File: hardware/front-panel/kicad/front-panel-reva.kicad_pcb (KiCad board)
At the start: 2 copper layers, 184 x 62.3 mm, 35 parts, among them J1 UI_LINK / IDC 2x8 2.54mm, U1 TCA9534PWR

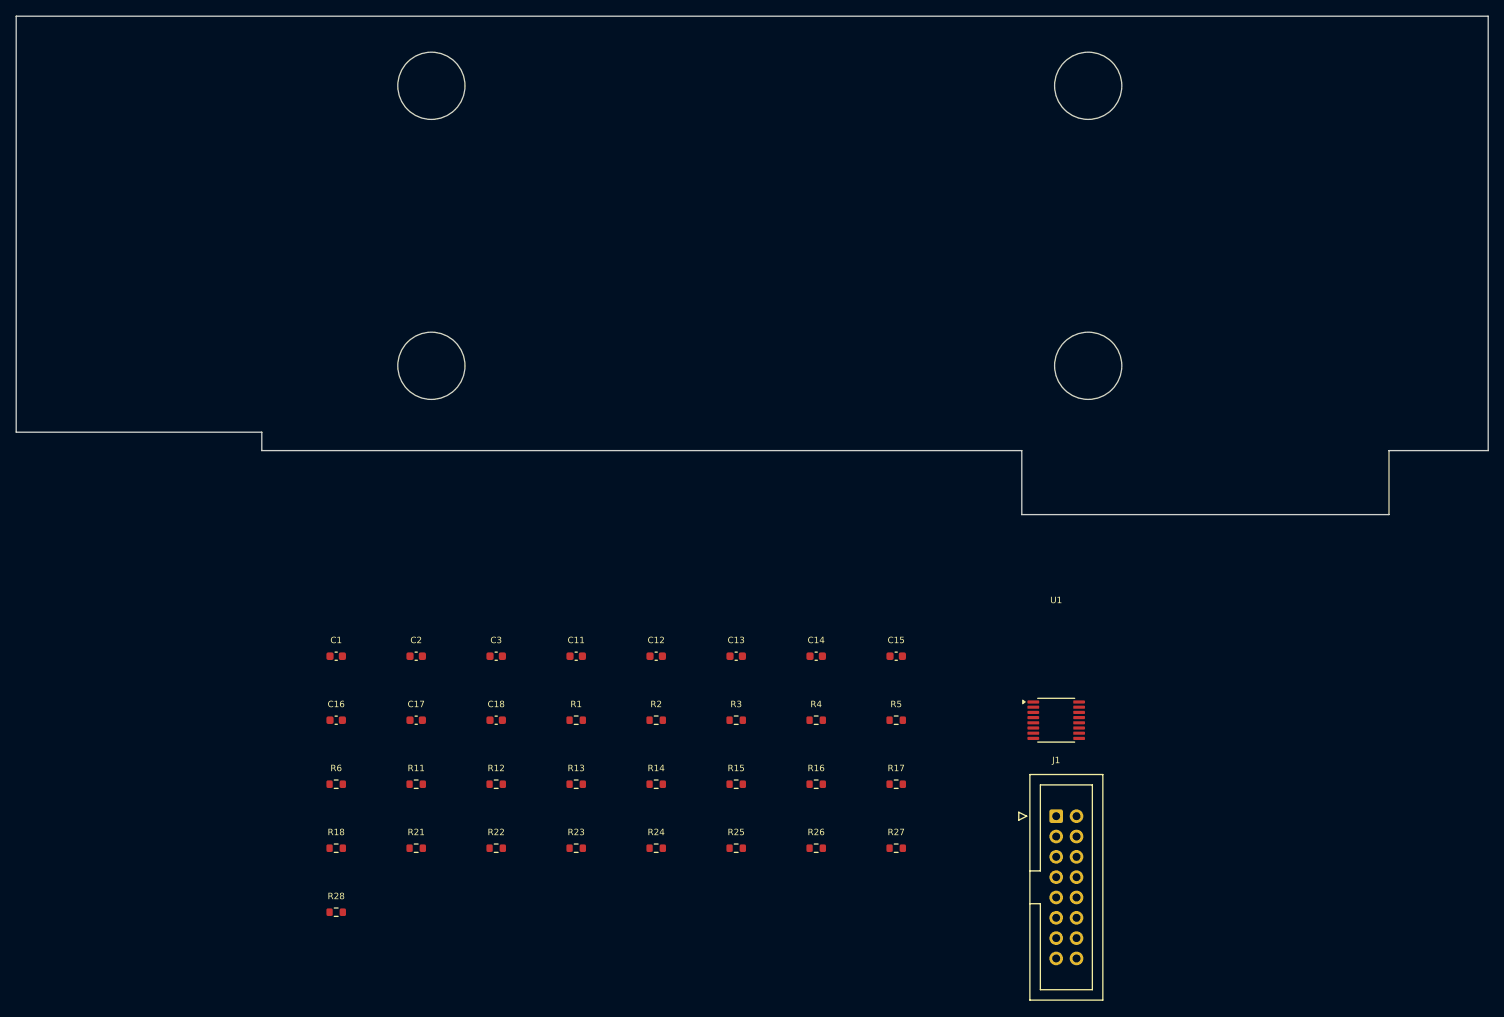
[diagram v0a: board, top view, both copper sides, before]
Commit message: Lay out and route the front panel PCB for JLCPCB
Assign JLC parts to the open positions: HRO K2-1102SP-A4SC-04 6x6x4.3 mm
switches (C83916) with a project footprint from the EasyEDA land pattern,
JST S8B-PH-K-S for J2 in the Waveshare cable order (C157915), and the
standby LED on TCA9534 P7 (KT-0603R + 470R). Seven key channels replace
the eighth, whose parts are removed from schematic and board.

layout_front_panel_pcb.py places the parts on the measured positions,
routes with Freerouting 2.4.1 through Specctra DSN/SES and pours GND on
both layers with stitching and island anchoring. KiCad 10.0.6 DRC with
schematic parity and all severities: 0 violations, 0 unconnected, 0
parity issues. export_front_panel_fab.py writes Gerbers, drill, BOM and
CPL for JLCPCB; the package stays a candidate pending the checks listed
in hardware/front-panel/layout.md.

Co-Authored-By: Claude Opus 5 <noreply@anthropic.com>
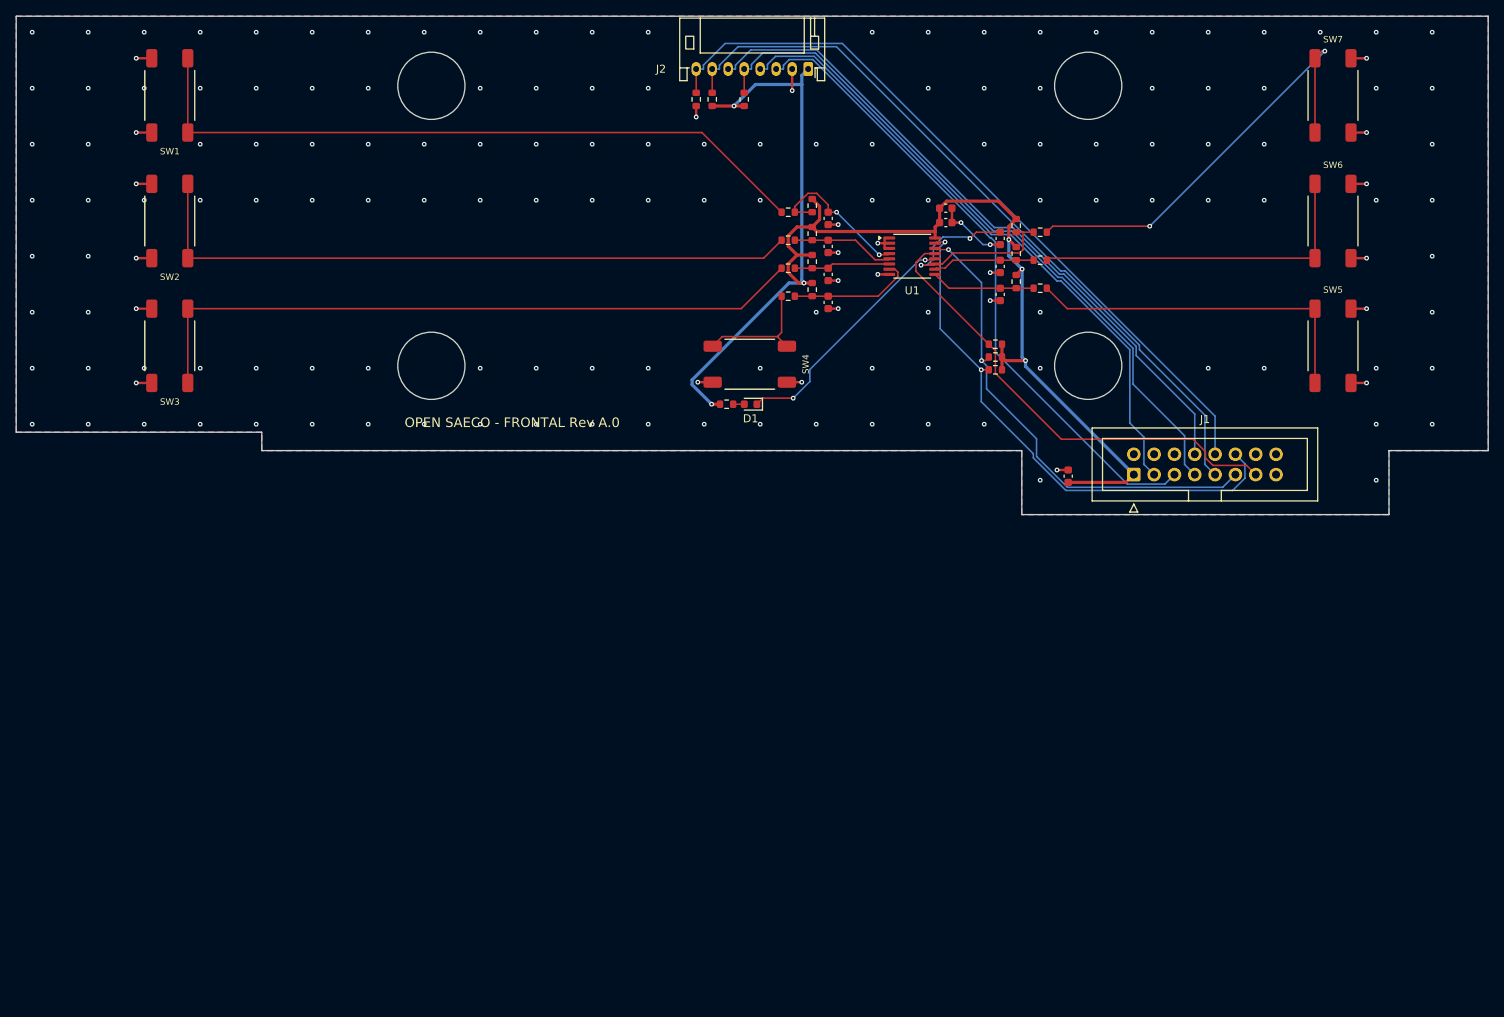
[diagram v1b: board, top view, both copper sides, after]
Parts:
- removed C18: 100nF / filtro, Capacitor_SMD:C_0603_1608Metric
- removed R18: 10k / pull-up, Resistor_SMD:R_0603_1608Metric
- removed R28: 1k / serie, Resistor_SMD:R_0603_1608Metric
- added D1: KT-0603R / STBY, LED_SMD:LED_0603_1608Metric, F.Cu at (91.8, 48.5)
- added J2: LCD_ADAPTER / JST PH 8, Connector_JST:JST_PH_S8B-PH-K_1x08_P2.00mm_Horizontal, F.Cu at (99.0, 6.60)
- added R7: 470 / LED, Resistor_SMD:R_0603_1608Metric, F.Cu at (88.8, 48.5)
- added SW1: KEY 1 / PB1, OpenSaeco:SW_HRO_K2-1102SP-A4SC-04, F.Cu at (19.2, 9.90)
- added SW2: KEY 2 / PB2, OpenSaeco:SW_HRO_K2-1102SP-A4SC-04, F.Cu at (19.2, 25.6)
- added SW3: KEY 3 / PB3, OpenSaeco:SW_HRO_K2-1102SP-A4SC-04, F.Cu at (19.2, 41.2)
- added SW4: KEY 4 / PB8, OpenSaeco:SW_HRO_K2-1102SP-A4SC-04, F.Cu at (91.7, 43.5)
- added SW5: KEY 5 / PB4/PB6, OpenSaeco:SW_HRO_K2-1102SP-A4SC-04, F.Cu at (164.6, 41.2)
- added SW6: KEY 6 / PB5, OpenSaeco:SW_HRO_K2-1102SP-A4SC-04, F.Cu at (164.6, 25.6)
- added SW7: KEY 7 / PB7, OpenSaeco:SW_HRO_K2-1102SP-A4SC-04, F.Cu at (164.6, 9.90)
- moved C16 100.5 mm to (123.0, 31.3), turned to -90 degrees
- moved R6 96.7 mm to (85.0, 10.4), turned to -90 degrees
- moved C17 94.6 mm to (123.0, 27.8), turned to -90 degrees
- moved C1 93.5 mm to (116.2, 25.8)
- moved R21 92.1 mm to (96.5, 24.5), turned to 180 degrees
- moved R11 87.6 mm to (99.5, 23.7), turned to -90 degrees
- moved C2 86.7 mm to (116.2, 24.0)
- moved R22 84.3 mm to (96.5, 28.0), turned to 180 degrees
- moved R5 80.9 mm to (87.0, 10.4), turned to 90 degrees
- moved R25 79.6 mm to (128.0, 34.0)
- moved R12 79.4 mm to (99.5, 27.2), turned to -90 degrees
- moved R27 79.1 mm to (128.0, 27.0)
- moved R26 78.7 mm to (128.0, 30.5)
- moved R4 78.1 mm to (91.0, 10.4), turned to 90 degrees
- moved R23 77.2 mm to (96.5, 31.5), turned to 180 degrees
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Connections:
- U1 pad 12: /KEY_8_N -> /LED_STBY_N
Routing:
- net /3V3_UI: track 0.00 -> 170.1 mm, vias 0 -> 6
- net /LCD_BL_PWM: track 0.00 -> 93.5 mm
- net /LCD_RST_N: track 0.00 -> 93.4 mm
- net /SW_1_RAW: track 0.00 -> 87.6 mm
- net /LCD_CS_N: track 0.00 -> 87.0 mm
- net /SW_3_RAW: track 0.00 -> 85.6 mm
- net /SW_2_RAW: track 0.00 -> 84.4 mm
- net /LCD_DC: track 0.00 -> 84.1 mm
- net /LCD_MOSI: track 0.00 -> 81.1 mm
- net /LCD_SCLK: track 0.00 -> 79.3 mm
- net /KEY_SDA: track 0.00 -> 66.6 mm, vias 0 -> 2
- net /KEY_SCL: track 0.00 -> 60.4 mm, vias 0 -> 2
- net /KEY_INT_N: track 0.00 -> 59.1 mm
- net /SW_7_RAW: track 0.00 -> 55.0 mm, vias 0 -> 2
- net /GND_UI: track 0.00 -> 53.2 mm, vias 0 -> 164
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- added copper zone on B.Cu, net /GND_UI
- added copper zone on F.Cu, net /GND_UI
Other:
- board text added: "JLCJLCJLCJLC"
- board text added: "OPEN SAECO - FRONTAL Rev A.0"

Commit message: Enter every harness connector from the top
The owner wants every wire-to-board header vertical, to free the board
area the side-entry housings took. The JST S-series headers become their
B-series twins: B2B-XH-A on J101, J105, J107 and J112, B3B-XH-A on J106,
B5B-XH-A on J113, B8B-XH-A on J108, B3B-PH-K-S on J109, B2P-VH on J117,
B3P-VH on J115 and J118, and B8B-PH-K-S on the front panel's J2. All are
in stock at JLCPCB; the assembly type is still to be confirmed.

KiCad's footprints for both series share pad position, pitch and drill,
so each part keeps its origin and rotation and the copper is untouched.
The one exception is J118: the vertical VH housing reaches 4.2 mm north
of its pins and hit PS701's courtyard by 0.6 mm, so it drops 0.8 mm, well
within JP17's 1.5 mm tolerance, and its three track stubs follow.

The courtyards give back about 750 mm2 on the main board, the useful part
beside J107/J108 and under J101/J112. ERC is clean on both boards. The
main board's DRC is unchanged: two intentional dangling ends, 77 open
connections and the three mounting-hole parity notes. The front panel
has no violations once its ground pour is refilled.

Co-Authored-By: Claude Opus 5 <noreply@anthropic.com>
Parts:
- J2: footprint Connector_JST:JST_PH_S8B-PH-K_1x08_P2.00mm_Horizontal -> Connector_JST:JST_PH_B8B-PH-K_1x08_P2.00mm_Vertical

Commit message: Fit the owner-identified Wurth WR-MM front-panel link on both boards
The owner identified the connector of the original link between the main
board and the front panel as Wurth WR-MM 690367181672 (16 contacts at
1.27 mm stagger), the same part at both ends of a 1:1 16-wire flat cable.
The latch of the cable plug enters a 1.5 mm hole beside pin 1, which locks
it and sets its direction, so pin 1 always meets pin 1. It replaces the
2x8 IDC in J104 and J1. JLCPCB lists it as C19103863, without stock.

The footprint follows Wurth drawing 690367181672 rev 002.000: 0.85 mm
holes, 1.4 mm pads, a 22.32 x 5 mm body and the 1.5 mm non-plated latch
hole; it gets a 6.1 mm tall stand-in model shared by both boards.

- Main board: J104 turns 180 deg with pin 1 on the IDC's pin 1, so the
  odd pins stay and the even pins move 1.27 mm east. 3V3_UI passes west of
  the latch hole; DC, BL and SDA reach their new pins and SCL and INT end on
  the pad centres. 1315 segments, 439 vias.
- Front panel: J1 is centred on the original JP3 zone, C3 stays by pin 1,
  rerouted by Freerouting (297 segments, 192 vias); fab package refreshed.

The photo count of 20 contacts for JP21 was wrong. ERC 0 on both boards;
netlists 187/612 and 42/118. DRC with all severities: main 0 violations,
0 unconnected, parity only MH1-MH3; front 0/0/0. Still to do: try the
cable latch in both new boards; 3V3_UI rides one 1.5 A contact.

Co-Authored-By: Claude Opus 5.5 <noreply@anthropic.com>
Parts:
- J1: value UI_LINK / IDC 2x8 2.54mm -> UI_LINK / WR-MM 16; footprint Connector_IDC:IDC-Header_2x08_P2.54mm_Vertical -> OpenSaeco:Wurth_WR-MM_690367181672_2x08_P1.27mm_Vertical
- moved C3 10.3 mm to (141.8, 57.5)
- moved J1 5.43 mm to (145.1, 56.7), turned to 180 degrees
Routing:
- net /GND_UI: track 53.2 -> 151.7 mm, vias 164 -> 168
- net /LCD_RST_N: track 93.4 -> 105.9 mm
- net /3V3_UI: track 170.1 -> 181.7 mm, vias 6 -> 8
- net /LCD_MOSI: track 81.1 -> 89.7 mm
- net /KEY_7_N: track 30.6 -> 23.9 mm
- net /KEY_INT_N: track 59.1 -> 64.3 mm, vias 0 -> 1
- net /KEY_SDA: track 66.6 -> 61.9 mm
- net /KEY_SCL: track 60.4 -> 64.2 mm
- net /LCD_DC: track 84.1 -> 85.0 mm
- net /LCD_SCLK: track 79.3 -> 80.0 mm, vias 0 -> 1
- net /LCD_CS_N: track 87.0 -> 87.4 mm, vias 0 -> 1
- net /LCD_BL_PWM: vias 0 -> 1
